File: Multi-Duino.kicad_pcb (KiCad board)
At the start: 4 copper layers, 68.6 x 53.3 mm, 67 parts, among them J1 M20-9980345, J10 Micro_SD_Card_Det1, J2 M20-9980245, J3 M20-9980345, J4 PPTC101LFBN-RC, J5 PPTC081LFBN-RC, J6 PPTC061LFBN-RC, J7 PPTC081LFBN-RC, J8 USB_C_Receptacle_USB2.0_16P, Q1 FDN340P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

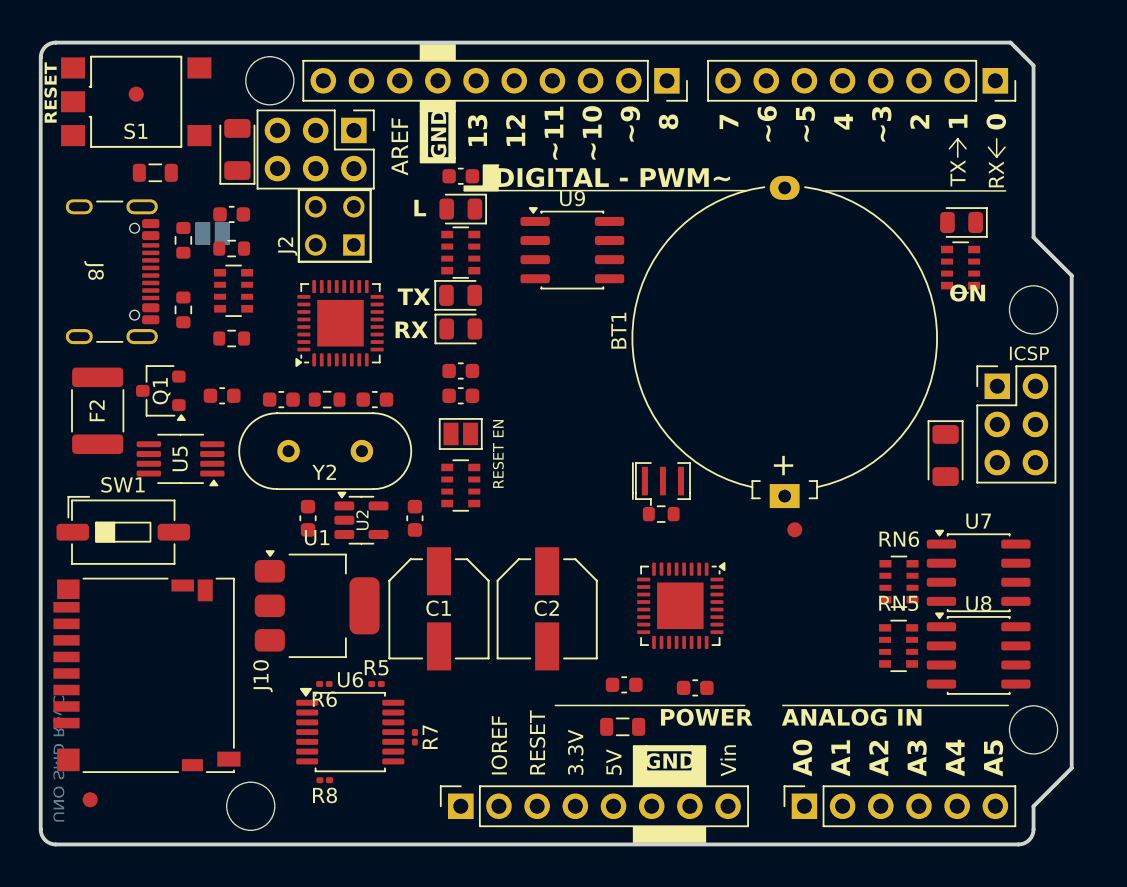
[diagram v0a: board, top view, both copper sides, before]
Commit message: Update Multiduino v2 design
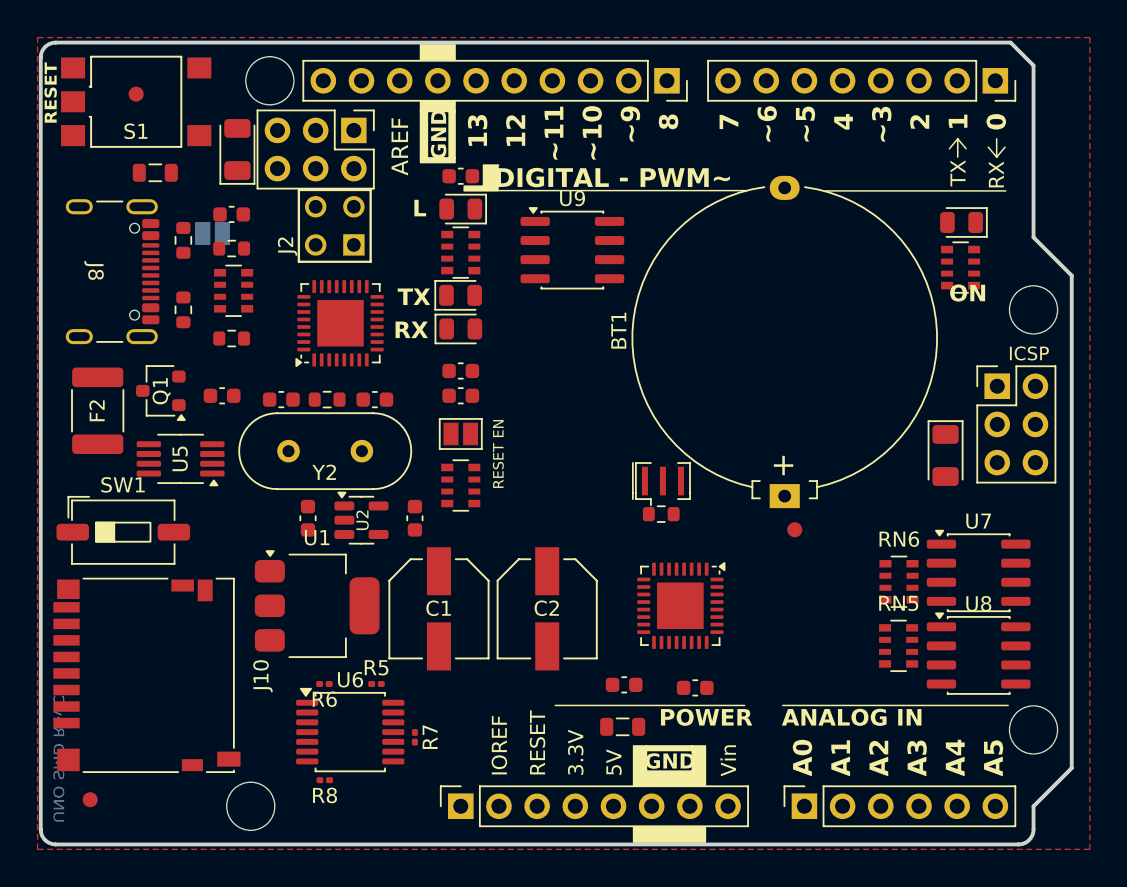
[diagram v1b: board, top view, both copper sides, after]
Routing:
- added copper zone on F.Cu, net GND
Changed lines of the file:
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@@
+		)
+	)
+	(zone
+		(net 1)
+		(net_name "GND")
+		(layer "F.Cu")
+		(hatch none 0.5)
+		(connect_pads yes
+			(clearance 0.3)
+		)
+		(min_thickness 0.25)
+		(filled_areas_thickness no)
+		(fill yes
+			(thermal_gap 0.5)
+			(thermal_bridge_width 0.5)
+		)
+		(polygon
+			(pts
+				(xy 114 78) (xy 184 78) (xy 184 132) (xy 114 132)
+			)
 		)
 	)

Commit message: Update Multiduino v2 design
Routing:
- added copper zone on B.Cu, net +5V
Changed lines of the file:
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@@
+		)
+	)
+	(zone
+		(net 2)
+		(net_name "+5V")
+		(layer "B.Cu")
+		(hatch none 0.5)
+		(connect_pads yes
+			(clearance 0.3)
+		)
+		(min_thickness 0.25)
+		(filled_areas_thickness no)
+		(fill yes
+			(thermal_gap 0.5)
+			(thermal_bridge_width 0.5)
+		)
+		(polygon
+			(pts
+				(xy 113.5 77.5) (xy 184.5 77.5) (xy 184.5 132.5) (xy 113.5 132.5)
+			)
 		)
 	)
